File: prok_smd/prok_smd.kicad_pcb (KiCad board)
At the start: 2 copper layers, 107.5 x 41.3 mm, 52 parts, among them CON1 microSD_Card, J1 POWER, J12 Conn_01x05_Male, J17 Conn_01x05_Male, J2 Conn_01x05_Female, J5 TIME_CV, J6 CHANNEL_CV, J7 RESET_CV, J8 OUT, J9 Conn_01x05_Female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

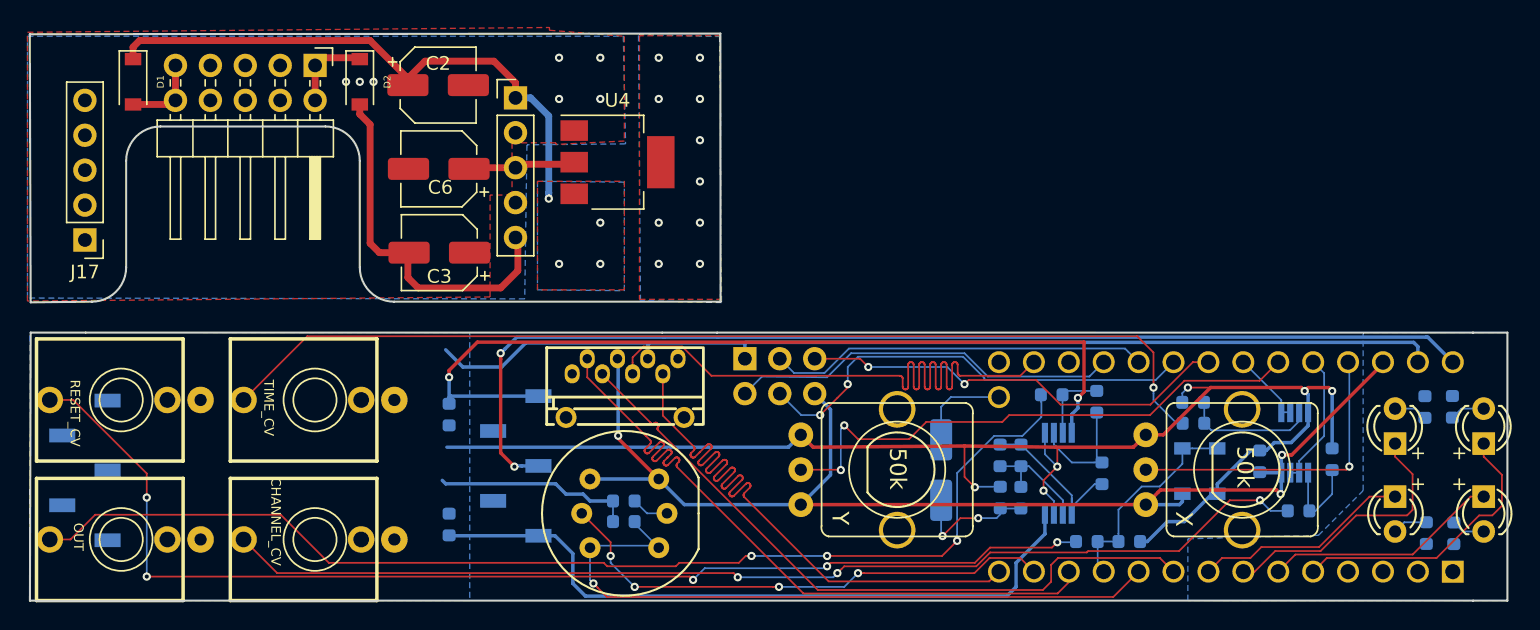
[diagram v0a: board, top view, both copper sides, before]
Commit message: :zap: Added Either way power and more rugged fixations
same
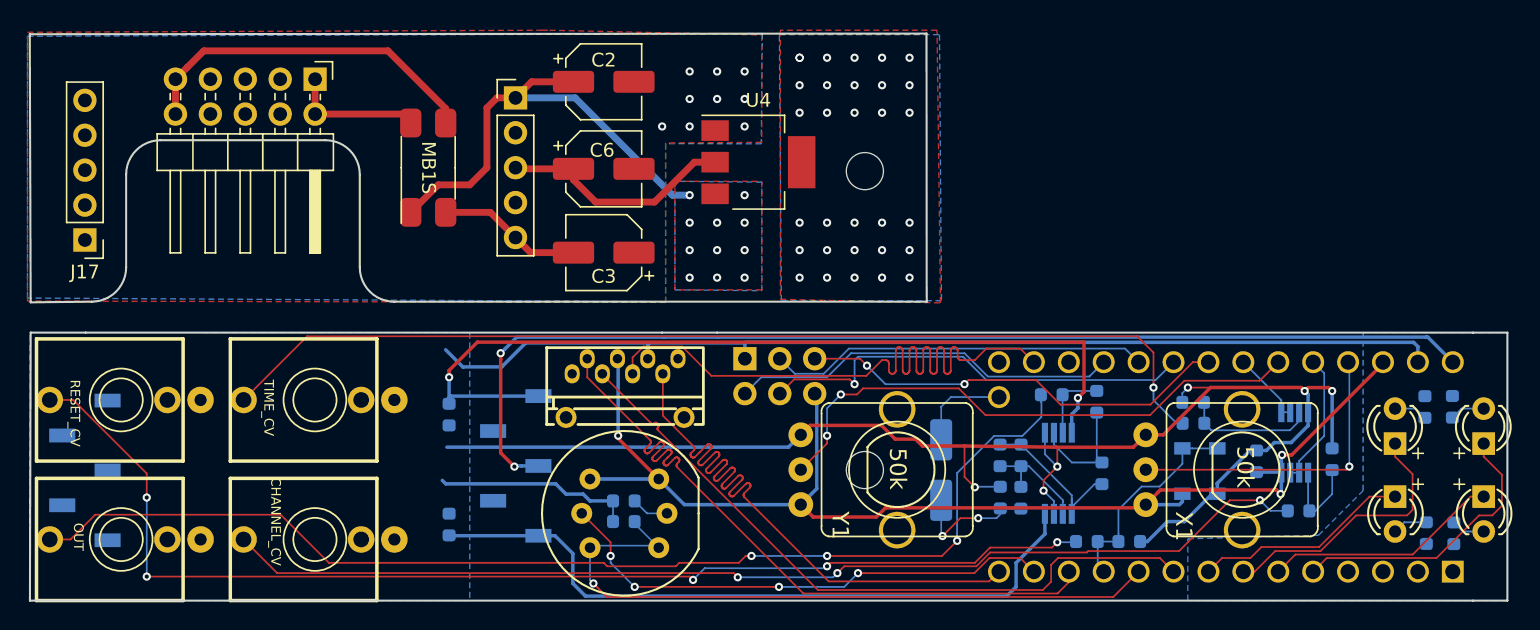
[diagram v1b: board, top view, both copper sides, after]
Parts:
- removed D2: 1N5819, Diode_SMD:D_SOD-123
- added H1: MountingHole, MountingHole:MountingHole_2.7mm_M2.5, F.Cu at (160.8, 65.0)
- added H2: MountingHole, MountingHole:MountingHole_2.7mm_M2.5, F.Cu at (160.8, 43.2)
- D1: value 1N5819 -> MB1S; footprint Diode_SMD:D_SOD-123 -> NN_Footprints:SOIC-4-POWER
- moved D1 22.4 mm to (129.0, 43.0), turned to 90 degrees
- moved C2 12.1 mm to (141.8, 36.8)
- moved C6 12.0 mm to (141.8, 43.1), turned to 0 degrees
- moved C3 12.0 mm to (141.8, 49.2)
- moved U4 10.2 mm to (153.0, 42.6)
- moved J1 1.00 mm to (120.7, 36.6)
- moved C1 0.23 mm to (189.2, 64.4)
- renumbered X to X1, Y to Y1
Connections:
- D1 pad 2: Net-(D1-Pad2) -> -12V
- J1 pad 1: Net-(D2-Pad1) -> Net-(D1-Pad4)
- J1 pad 10: Net-(D1-Pad2) -> Net-(D1-Pad3)
- J1 pad 2: Net-(D2-Pad1) -> Net-(D1-Pad4)
- J1 pad 9: Net-(D1-Pad2) -> Net-(D1-Pad3)
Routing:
- net Net-(D1-Pad3): track 0.00 -> 25.8 mm
- net -12V: track 77.5 -> 61.3 mm
- net Net-(D1-Pad4): track 0.00 -> 9.77 mm
- net +5V: track 88.8 -> 98.2 mm
- net +12V: track 105.7 -> 97.7 mm, vias 6 -> 13
- net Net-(D2-Pad1): track 6.06 -> 0.00 mm
- net Net-(D1-Pad2): track 5.75 -> 0.00 mm
- net A4: track 33.3 -> 32.3 mm, vias 2 -> 1
- net GND: track 196.9 -> 197.4 mm, vias 13 -> 15
- net TIME_POT: track 40.6 -> 41.1 mm
- net Net-(HS1-Pad1): vias 10 -> 31
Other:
- outline, holes or cut-outs redrawn
- board text added: "EITHER WAY"

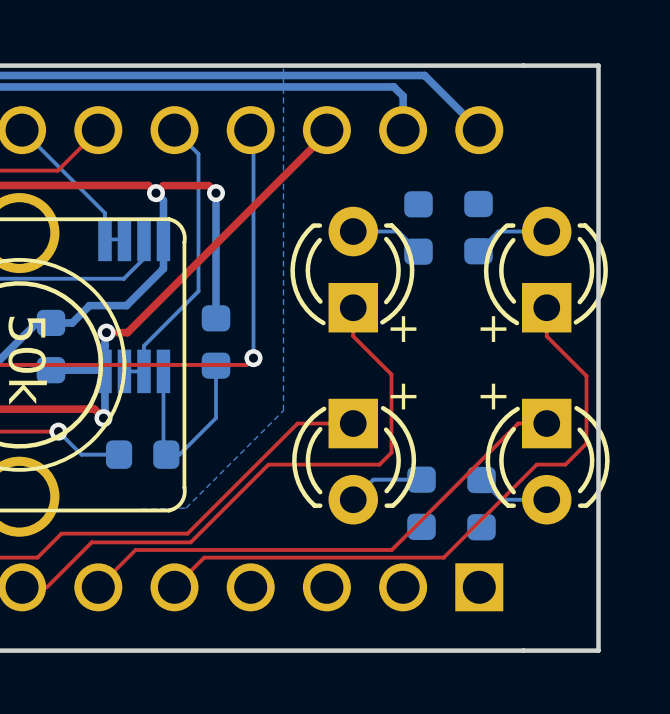
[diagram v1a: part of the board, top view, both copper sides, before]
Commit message: :construction: Add some caps to smoothe PWM
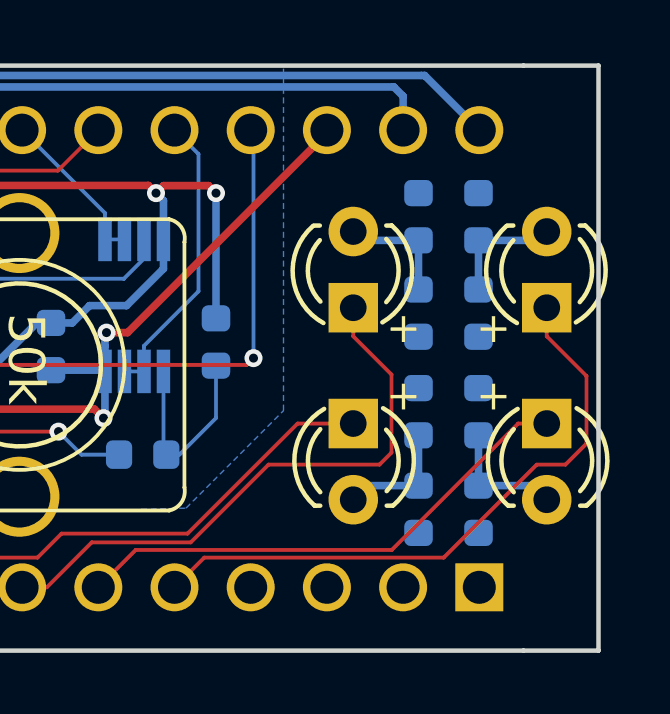
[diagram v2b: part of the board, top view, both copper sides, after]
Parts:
- added C10: 10nF, Capacitor_SMD:C_0603_1608Metric, B.Cu at (201.5, 63.2)
- added C11: 10nF, Capacitor_SMD:C_0603_1608Metric, B.Cu at (203.5, 66.5)
- added C12: 10nF, Capacitor_SMD:C_0603_1608Metric, B.Cu at (203.5, 63.2)
- added C9: 10nF, Capacitor_SMD:C_0603_1608Metric, B.Cu at (201.5, 66.5)
- moved R15 0.38 mm to (201.5, 60.0)
- moved R13 0.36 mm to (203.5, 60.0)
- moved R16 0.22 mm to (201.5, 69.8)
- moved R14 0.21 mm to (203.5, 69.8)
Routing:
- net Net-(C11-Pad1): track 2.45 -> 4.14 mm
- net Net-(C9-Pad1): track 2.55 -> 4.04 mm
- net Net-(C12-Pad1): track 2.55 -> 4.03 mm
- net Net-(C10-Pad1): track 2.45 -> 3.93 mm

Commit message: :recycle: Redid routing
same


same


same
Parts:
- removed D3, D4: D, Diode_SMD:D_SOD-123
- removed H1, H2: MountingHole, MountingHole:MountingHole_2.7mm_M2.5
- added D2: BAT54S, Package_TO_SOT_SMD:SOT-23, B.Cu at (185.0, 65.0)
- moved C3 12.8 mm to (129.0, 49.0), turned to 0 degrees
- moved C6 12.2 mm to (129.6, 43.1), turned to 180 degrees
- moved U4 9.77 mm to (143.8, 45.8), turned to 270 degrees
- moved D1 6.62 mm to (127.8, 36.5), turned to 180 degrees
- moved C2 1.77 mm to (143.0, 38.0)
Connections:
- J2 pad 4: GND -> GNDA
- J2 pad 5: GND -> GNDA
- J8 pad S: GND -> GNDA
- R1 pad 1: GND -> GNDA
- U3 pad 3: GND -> GNDA
- U3 pad 5: GND -> GNDA
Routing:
- net GND: track 197.4 -> 96.6 mm, vias 15 -> 11
- net GNDA: track 0.00 -> 85.2 mm, vias 0 -> 6
- net +12V: track 97.7 -> 68.4 mm, vias 13 -> 6
- net -12V: track 61.3 -> 82.7 mm, vias 0 -> 2
- net Net-(J5-PadT): track 74.9 -> 84.6 mm, vias 1 -> 4
- net Net-(D1-Pad3): track 25.8 -> 17.8 mm
- net +3V3: track 89.4 -> 94.0 mm, vias 3 -> 2
- net RESET_CV: track 15.9 -> 12.6 mm
- net Net-(D1-Pad4): track 9.77 -> 6.80 mm
- net CHANNEL_POT: track 22.5 -> 20.2 mm
- net +5V: track 98.2 -> 95.9 mm, vias 2 -> 3
- net LED_RESET: track 37.3 -> 35.6 mm, vias 4 -> 3
- net Net-(J8-PadT): track 83.5 -> 84.2 mm, vias 3 -> 0
- net TIME_POT: track 41.1 -> 41.8 mm
- net Net-(J7-PadT): track 85.6 -> 85.3 mm, vias 5 -> 4
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- added copper zone on B.Cu, net GNDA
- added copper zone on F.Cu, net GNDA
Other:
- outline, holes or cut-outs redrawn

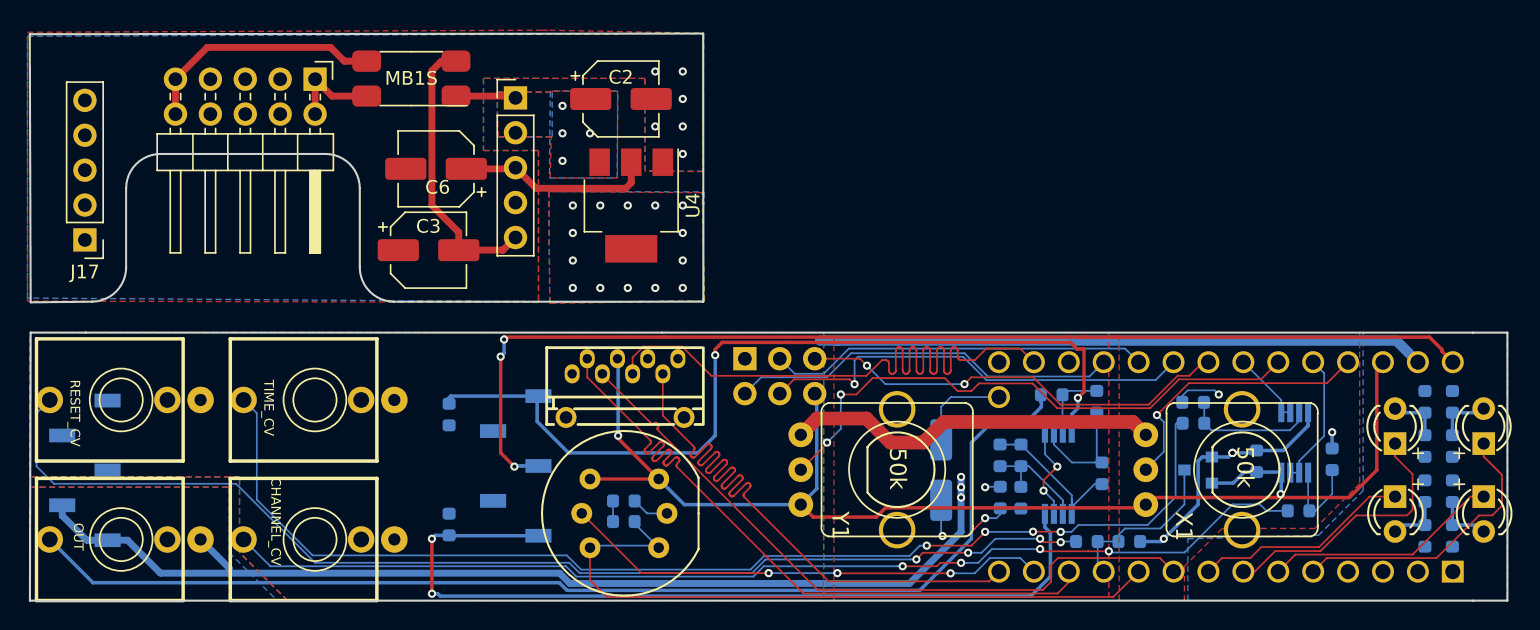
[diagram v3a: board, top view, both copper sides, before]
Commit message: :truck: :lipstick: Move CV circuitry back, and clean PCB
same
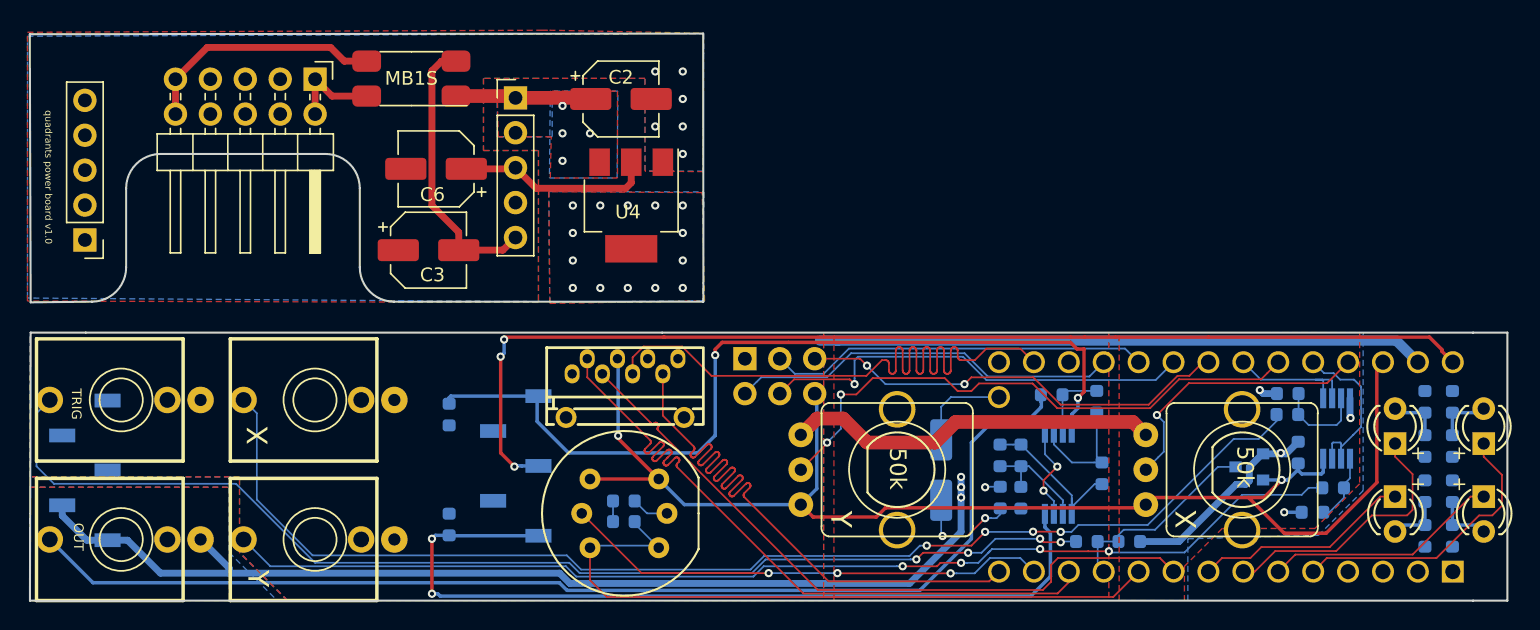
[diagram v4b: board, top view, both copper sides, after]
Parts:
- added G***: LOGO, NN_Footprints:nebularnoise_logo, B.Cu at (111.3, 65.0)
- added G***: LOGO, NN_Footprints:caution_hot, B.Cu at (143.5, 47.5)
- added G***: LOGO, NN_Footprints:nebularnoise_logo, B.Cu at (129.5, 46.5)
- moved R8 6.91 mm to (191.5, 59.4)
- moved R6 6.86 mm to (191.5, 61.0)
- moved R9 4.12 mm to (193.3, 68.1), turned to 0 degrees
- moved D2 3.73 mm to (188.7, 64.8)
- moved U2 3.21 mm to (195.1, 62.0)
- moved C1 3.09 mm to (192.3, 63.7)
- moved R7 3.02 mm to (194.8, 66.3)
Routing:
- net +12V: track 68.4 -> 73.9 mm
- net +3V3: track 94.0 -> 99.2 mm
- net TIME_CV_ADC: track 5.44 -> 10.2 mm
- net Net-(J5-PadT): track 84.6 -> 88.9 mm
- net GND: track 96.6 -> 92.7 mm, vias 11 -> 10
- net CHANNEL_CV_ADC: track 9.78 -> 13.0 mm
- net TIME_CV: track 9.57 -> 6.72 mm
- net Net-(J6-PadT): track 79.8 -> 82.6 mm
- net RESET_CV: track 12.6 -> 14.9 mm
- net CHANNEL_CV: track 6.72 -> 4.70 mm
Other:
- board text added: "Adapted from a design by Tom Whitwell"
- board text added: "CAUTION HOT"
- board text added: "Quadrants"
- board text added: "RED EITHER WAY"
- board text added: "TRANS RIGHTS"
- board text added: "TRIG"
- board text added: "X"
- board text added: "Y"
- board text added: "github.com /nebularnoise /quadrants"
- board text added: "github.com/nebularnoise/quadrants"
- board text added: "quadrants main board v1.0"
- board text added: "quadrants power board v1.0"
- board text removed: "EITHER WAY"
